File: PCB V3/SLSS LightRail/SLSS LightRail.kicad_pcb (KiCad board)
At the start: 2 copper layers, 1 part

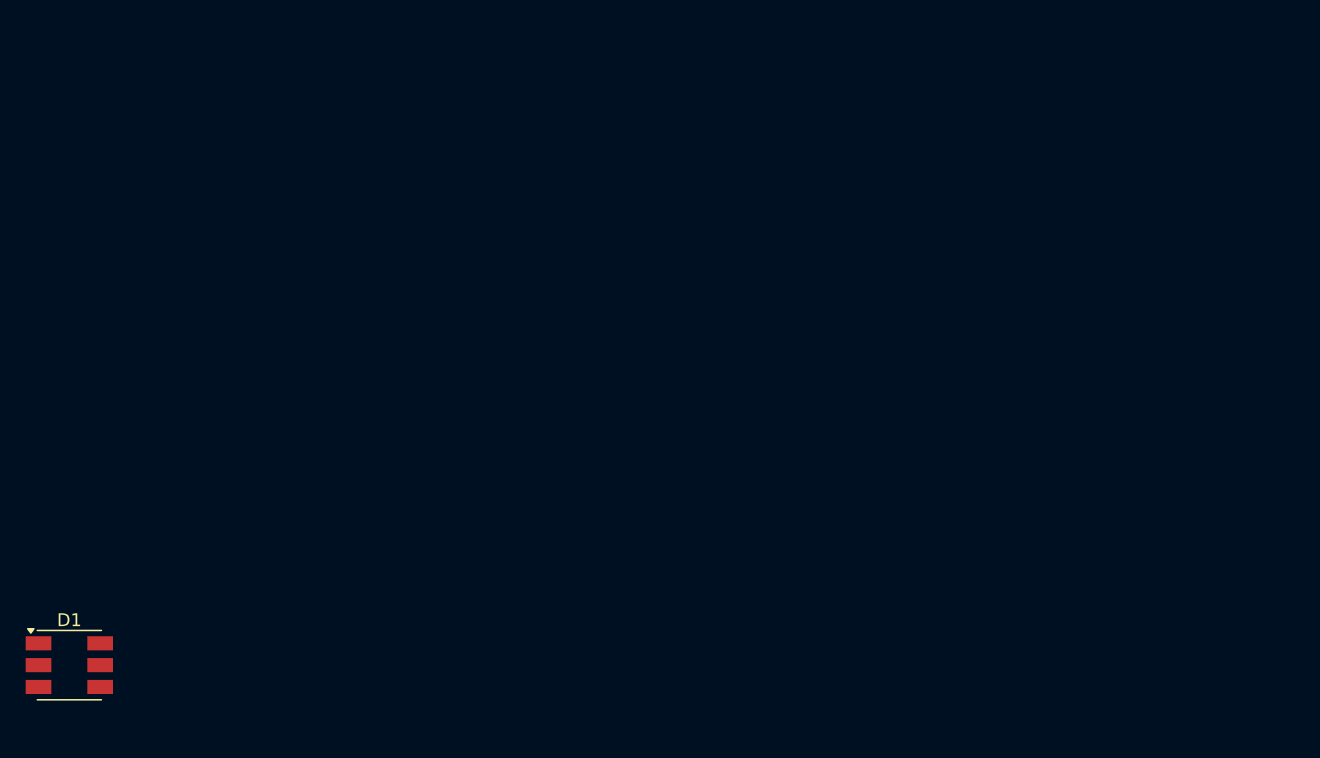
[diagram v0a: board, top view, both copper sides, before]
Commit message: Minor alterations to LED PCB
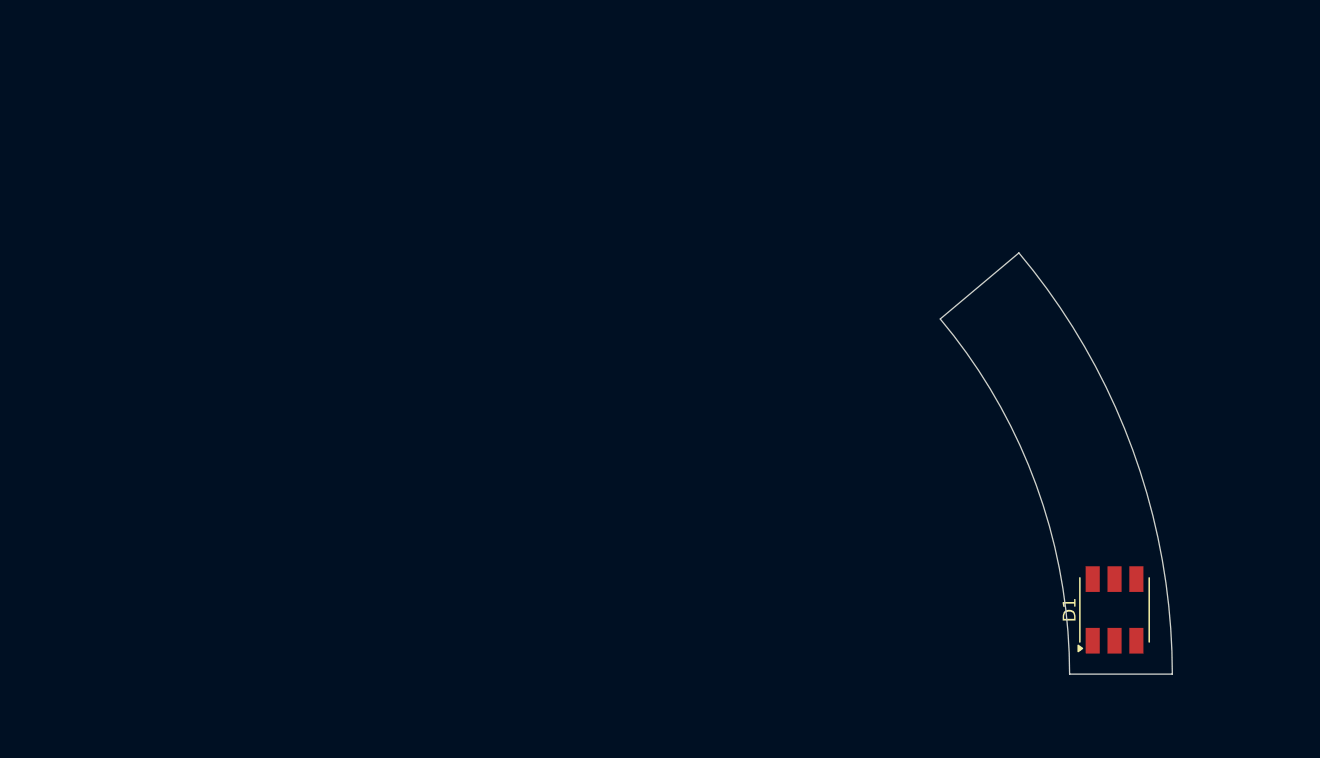
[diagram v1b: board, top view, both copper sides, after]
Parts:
- moved D1 81.5 mm to (196.5, 95.0), turned to 90 degrees
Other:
- board outline added: 18.1 x 32.8 mm
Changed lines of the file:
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@@
 	(footprint "LED_SMD:LED_RGB_5050-6"
 		(layer "F.Cu")
-		(at 115.1 99.3)
+		(at 196.5 95 90)
 		(descr "http://cdn.sparkfun.com/datasheets/Components/LED/5060BRG4.pdf")
 		(tags "RGB LED 5050-6")
 		(property "Reference" "D1"
-			(at 0 -3.5 180)
+			(at 0 -3.5 90)
 			(layer "F.SilkS")
 			(effects
@@
 		)
 		(property "Value" "LED_RGB"
-			(at 0 3.3 0)
+			(at 0 3.3 90)
 			(layer "F.Fab")
 			(effects
@@
 		)
 		(property "Datasheet" "~"
-			(at 0 0 0)
+			(at 0 0 90)
 			(unlocked yes)
 			(layer "F.Fab")
@@
 		)
 		(property "Description" "RGB LED, 6 pin package"
-			(at 0 0 0)
+			(at 0 0 90)
 			(unlocked yes)
 			(layer "F.Fab")
@@
 		)
 		(fp_line
+			(start 3.65 -2.75)
+			(end -3.65 -2.75)
+			(stroke
+				(width 0.05)
+				(type solid)
+			)
+			(layer "F.CrtYd")
+		)
+		(fp_line
 			(start -3.65 -2.75)
 			(end -3.65 2.75)
@@
 		)
 		(fp_line
+			(start 3.65 2.75)
+			(end 3.65 -2.75)
+			(stroke
+				(width 0.05)
+				(type solid)
+			)
+			(layer "F.CrtYd")
+		)
+		(fp_line
 			(start -3.65 2.75)
 			(end 3.65 2.75)
@@
 		)
 		(fp_line
-			(start 3.65 -2.75)
-			(end -3.65 -2.75)
-			(stroke
-				(width 0.05)
-				(type solid)
-			)
-			(layer "F.CrtYd")
-		)
-		(fp_line
-			(start 3.65 2.75)
-			(end 3.65 -2.75)
-			(stroke
-				(width 0.05)
-				(type solid)
-			)
-			(layer "F.CrtYd")
+			(start 2.5 -2.5)
+			(end -2.5 -2.5)
+			(stroke
+				(width 0.1)
+				(type solid)
+			)
+			(layer "F.Fab")
 		)
 		(fp_line
@@
 		)
 		(fp_line
+			(start 2.5 2.5)
+			(end 2.5 -2.5)
+			(stroke
+				(width 0.1)
+				(type solid)
+			)
+			(layer "F.Fab")
+		)
+		(fp_line
 			(start -2.5 2.5)
 			(end 2.5 2.5)
-			(stroke
-				(width 0.1)
-				(type solid)
-			)
-			(layer "F.Fab")
-		)
-		(fp_line
-			(start 2.5 -2.5)
-			(end -2.5 -2.5)
-			(stroke
-				(width 0.1)
-				(type solid)
-			)
-			(layer "F.Fab")
-		)
-		(fp_line
-			(start 2.5 2.5)
-			(end 2.5 -2.5)
 			(stroke
 				(width 0.1)
@@
 		)
 		(fp_text user "${REFERENCE}"
-			(at 0 0 0)
+			(at 0 0 90)
 			(layer "F.Fab")
 			(effects
@@
 		)
 		(pad "1" smd rect
-			(at -2.4 -1.7 90)
+			(at -2.4 -1.7 180)
 			(size 1.1 2)
 			(layers "F.Cu" "F.Mask" "F.Paste")
@@
 		)
 		(pad "2" smd rect
-			(at -2.4 0 90)
+			(at -2.4 0 180)
 			(size 1.1 2)
 			(layers "F.Cu" "F.Mask" "F.Paste")
@@
 		)
 		(pad "3" smd rect
-			(at -2.4 1.7 90)
+			(at -2.4 1.7 180)
 			(size 1.1 2)
 			(layers "F.Cu" "F.Mask" "F.Paste")
@@
 		)
 		(pad "4" smd rect
-			(at 2.4 1.7 90)
+			(at 2.4 1.7 180)
 			(size 1.1 2)
 			(layers "F.Cu" "F.Mask" "F.Paste")
@@
 		)
 		(pad "5" smd rect
-			(at 2.4 0 90)
+			(at 2.4 0 180)
 			(size 1.1 2)
 			(layers "F.Cu" "F.Mask" "F.Paste")
@@
 		)
 		(pad "6" smd rect
-			(at 2.4 -1.7 90)
+			(at 2.4 -1.7 180)
 			(size 1.1 2)
 			(layers "F.Cu" "F.Mask" "F.Paste")
@@
 		)
 	)
+	(gr_line
+		(start 193 100)
+		(end 201 100)
+		(stroke
+			(width 0.05)
+			(type default)
+		)
+		(layer "Edge.Cuts")
+	)
+	(gr_arc
+		(start 189.050948 67.197204)
+		(mid 197.919716 82.544319)
+		(end 201 100)
+		(stroke
+			(width 0.05)
+			(type default)
+		)
+		(layer "Edge.Cuts")
+	)
+	(gr_line
+		(start 182.925309 72.342741)
+		(end 189.050948 67.197206)
+		(stroke
+			(width 0.05)
+			(type default)
+		)
+		(layer "Edge.Cuts")
+	)
+	(gr_arc
+		(start 182.925309 72.34274)
+		(mid 190.402898 85.282464)
+		(end 193 100)
+		(stroke
+			(width 0.05)
+			(type default)
+		)
+		(layer "Edge.Cuts")
+	)
 	(embedded_fonts no)

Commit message: light rail PCB
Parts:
- added D2: LED_RGB, LED_SMD:LED_RGB_5050-6, F.Cu at (197.6, 86.3)
- added D3: LED_RGB, LED_SMD:LED_RGB_5050-6, F.Cu at (194.0, 75.8)
- added J1: Conn_01x04, Connector_JST:JST_GH_SM04B-GHS-TB_1x04-1MP_P1.25mm_Horizontal, F.Cu at (187.5, 66.4)
- added R1: 51R, Resistor_SMD:R_1206_3216Metric, F.Cu at (197.0, 91.5)
- added R2: 51R, Resistor_SMD:R_1206_3216Metric, F.Cu at (194.5, 81.0)
- added R3: 51R, Resistor_SMD:R_1206_3216Metric, F.Cu at (193.0, 71.5)
- added R4: 62R, Resistor_SMD:R_1206_3216Metric, F.Cu at (199.5, 91.5)
- added R5: 62R, Resistor_SMD:R_1206_3216Metric, F.Cu at (197.0, 81.0)
- added R6: 62R, Resistor_SMD:R_1206_3216Metric, F.Cu at (192.5, 69.0)
- added R7: 51R, Resistor_SMD:R_1206_3216Metric, F.Cu at (202.0, 91.5)
- added R8: 51R, Resistor_SMD:R_1206_3216Metric, F.Cu at (199.5, 81.0)
- added R9: 51R, Resistor_SMD:R_1206_3216Metric, F.Cu at (189.0, 73.0)
- moved D1 4.02 mm to (200.1, 96.8), turned to 0 degrees
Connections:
- D1 pad 1: unconnected-(D1-RK-Pad1) -> Net-(D1-RK)
- D1 pad 2: unconnected-(D1-GK-Pad2) -> Net-(D1-GK)
- D1 pad 3: unconnected-(D1-BK-Pad3) -> Net-(D1-BK)
- D1 pad 4: unconnected-(D1-BA-Pad4) -> Net-(D1-BA)
- D1 pad 5: unconnected-(D1-GA-Pad5) -> Net-(D1-GA)
- D1 pad 6: unconnected-(D1-RA-Pad6) -> Net-(D1-RA)
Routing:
- net Net-(J1-Pin_4): track 0.00 -> 47.2 mm
- net Net-(D1-BA): track 0.00 -> 41.7 mm, vias 0 -> 4
- net Net-(D1-GA): track 0.00 -> 41.0 mm, vias 0 -> 4
- net Net-(D1-RA): track 0.00 -> 39.9 mm, vias 0 -> 4
- net Net-(D2-BK): track 0.00 -> 7.58 mm
- net Net-(D1-BK): track 0.00 -> 7.55 mm
- net Net-(D2-GK): track 0.00 -> 5.25 mm
- net Net-(D1-GK): track 0.00 -> 5.25 mm
- net Net-(D2-RK): track 0.00 -> 2.39 mm
- net Net-(D1-RK): track 0.00 -> 2.39 mm
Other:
- board size 18.1 x 32.8 mm -> 24.9 x 39.6 mm
- board text added: "${REFERENCE}"

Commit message: Finished Lightrail PCB
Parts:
- moved R9 13.5 mm to (184.0, 60.5), turned to 0 degrees
- moved J1 12.1 mm to (178.3, 58.5), turned to -120 degrees
- moved R3 11.2 mm to (183.5, 65.5)
- moved R6 10.4 mm to (184.0, 63.0)
- moved D3 8.96 mm to (189.1, 68.3), turned to 90 degrees
- moved R2 6.26 mm to (191.5, 75.5), turned to -90 degrees
- moved R8 6.23 mm to (196.5, 75.5), turned to -90 degrees
- moved R5 6.23 mm to (194.0, 75.6), turned to -90 degrees
- moved D2 3.79 mm to (196.8, 82.6), turned to 90 degrees
- moved R1 2.06 mm to (196.5, 89.5), turned to -90 degrees
- moved R4 2.06 mm to (199.0, 89.5), turned to 90 degrees
- moved R7 2.06 mm to (201.5, 89.5), turned to -90 degrees
- moved D1 0.81 mm to (199.7, 96.1), turned to 90 degrees
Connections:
- D1 pad 1: Net-(D1-RK) -> Net-(D1-BK)
- D1 pad 2: Net-(D1-GK) -> Net-(D1-BK)
- D2 pad 1: Net-(D2-RK) -> Net-(D1-BK)
- D2 pad 2: Net-(D2-GK) -> Net-(D1-BK)
- D2 pad 3: Net-(D2-BK) -> Net-(D1-BK)
- D2 pad 4: Net-(D1-BA) -> Net-(D2-BA)
- D2 pad 5: Net-(D1-GA) -> Net-(D2-GA)
- D2 pad 6: Net-(D1-RA) -> Net-(D2-RA)
- D3 pad 1: Net-(D3-RK) -> Net-(D1-BK)
- D3 pad 2: Net-(D3-GK) -> Net-(D1-BK)
- D3 pad 3: Net-(D3-BK) -> Net-(D1-BK)
- D3 pad 4: Net-(D1-BA) -> Net-(D3-BA)
- D3 pad 5: Net-(D1-GA) -> Net-(D3-GA)
- D3 pad 6: Net-(D1-RA) -> Net-(D3-RA)
- J1 pad 1: Net-(D1-RA) -> Net-(J1-Pin_1)
- J1 pad 2: Net-(D1-GA) -> Net-(J1-Pin_2)
- J1 pad 3: Net-(D1-BA) -> Net-(J1-Pin_3)
- J1 pad 4: Net-(J1-Pin_4) -> Net-(D1-BK)
- R1 pad 1: Net-(D1-RK) -> Net-(J1-Pin_1)
- R1 pad 2: Net-(J1-Pin_4) -> Net-(D1-RA)
- R2 pad 1: Net-(D2-RK) -> Net-(J1-Pin_1)
- R2 pad 2: Net-(J1-Pin_4) -> Net-(D2-RA)
- R3 pad 1: Net-(D3-RK) -> Net-(J1-Pin_1)
- R3 pad 2: Net-(J1-Pin_4) -> Net-(D3-RA)
- R4 pad 1: Net-(J1-Pin_4) -> Net-(D1-GA)
- R4 pad 2: Net-(D1-GK) -> Net-(J1-Pin_2)
- R5 pad 1: Net-(D2-GK) -> Net-(J1-Pin_2)
- R5 pad 2: Net-(J1-Pin_4) -> Net-(D2-GA)
- R6 pad 1: Net-(D3-GK) -> Net-(J1-Pin_2)
- R6 pad 2: Net-(J1-Pin_4) -> Net-(D3-GA)
- R7 pad 1: Net-(D1-BK) -> Net-(J1-Pin_3)
- R7 pad 2: Net-(J1-Pin_4) -> Net-(D1-BA)
- R8 pad 1: Net-(D2-BK) -> Net-(J1-Pin_3)
- R8 pad 2: Net-(J1-Pin_4) -> Net-(D2-BA)
- R9 pad 1: Net-(D3-BK) -> Net-(J1-Pin_3)
- R9 pad 2: Net-(J1-Pin_4) -> Net-(D3-BA)
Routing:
- net Net-(J1-Pin_2): track 0.00 -> 48.3 mm, vias 0 -> 2
- net Net-(J1-Pin_4): track 47.2 -> 0.00 mm
- net Net-(J1-Pin_3): track 0.00 -> 46.3 mm, vias 0 -> 3
- net Net-(J1-Pin_1): track 0.00 -> 46.0 mm, vias 0 -> 2
- net Net-(D1-BA): track 41.7 -> 2.74 mm, vias 4 -> 0
- net Net-(D1-GA): track 41.0 -> 2.99 mm, vias 4 -> 0
- net Net-(D1-RA): track 39.9 -> 3.32 mm, vias 4 -> 0
- net Net-(D1-BK): track 7.55 -> 18.0 mm, vias 0 -> 10
- net Net-(D3-BA): track 0.00 -> 7.80 mm
- net Net-(D2-BK): track 7.58 -> 0.00 mm
- net Net-(D2-GK): track 5.25 -> 0.00 mm
- net Net-(D1-GK): track 5.25 -> 0.00 mm
- net Net-(D3-GA): track 0.00 -> 5.06 mm
- net Net-(D2-RA): track 0.00 -> 4.93 mm
- net Net-(D2-GA): track 0.00 -> 4.32 mm
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- added copper zone on B.Cu, net Net-(D1-BK)
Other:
- board size 24.9 x 39.6 mm -> 34 x 48.5 mm
- board text removed: "${REFERENCE}"

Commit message: PCB size fix
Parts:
- moved R3 1.58 mm to (182.0, 66.0)
- moved D2 1.36 mm to (195.5, 83.0)
- moved D3 1.20 mm to (188.2, 69.1)
- moved D1 1.20 mm to (198.5, 96.1)
- moved J1 1.12 mm to (177.8, 59.5)
- moved R1 1.12 mm to (195.5, 90.0)
- moved R4 1.12 mm to (198.0, 90.0)
- moved R7 1.12 mm to (200.5, 90.0)
- moved R2 1.00 mm to (190.5, 75.5)
- moved R5 1.00 mm to (193.0, 75.6)
- moved R8 1.00 mm to (195.5, 75.5)
- moved R6 0.50 mm to (184.0, 63.5)
- moved R9 0.50 mm to (184.0, 61.0)
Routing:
- net Net-(D1-BK): track 18.0 -> 92.3 mm, vias 10 -> 6
- net Net-(J1-Pin_3): track 46.3 -> 39.7 mm, vias 3 -> 2
- net Net-(J1-Pin_2): track 48.3 -> 52.2 mm, vias 2 -> 4
- net Net-(J1-Pin_1): track 46.0 -> 43.6 mm, vias 2 -> 4
- net Net-(D2-RA): track 4.93 -> 6.88 mm
- net Net-(D3-RA): track 2.00 -> 3.29 mm
- net Net-(D1-RA): track 3.32 -> 2.74 mm
- net Net-(D1-GA): track 2.99 -> 2.41 mm
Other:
- board size 34 x 48.5 mm -> 33.5 x 47.6 mm
